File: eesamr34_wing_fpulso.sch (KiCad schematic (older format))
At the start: 19 parts, among them J3 Conn_01x02_Male, P1 SolderJumper_3_Bridged12, Q1 BS250, U2 4069

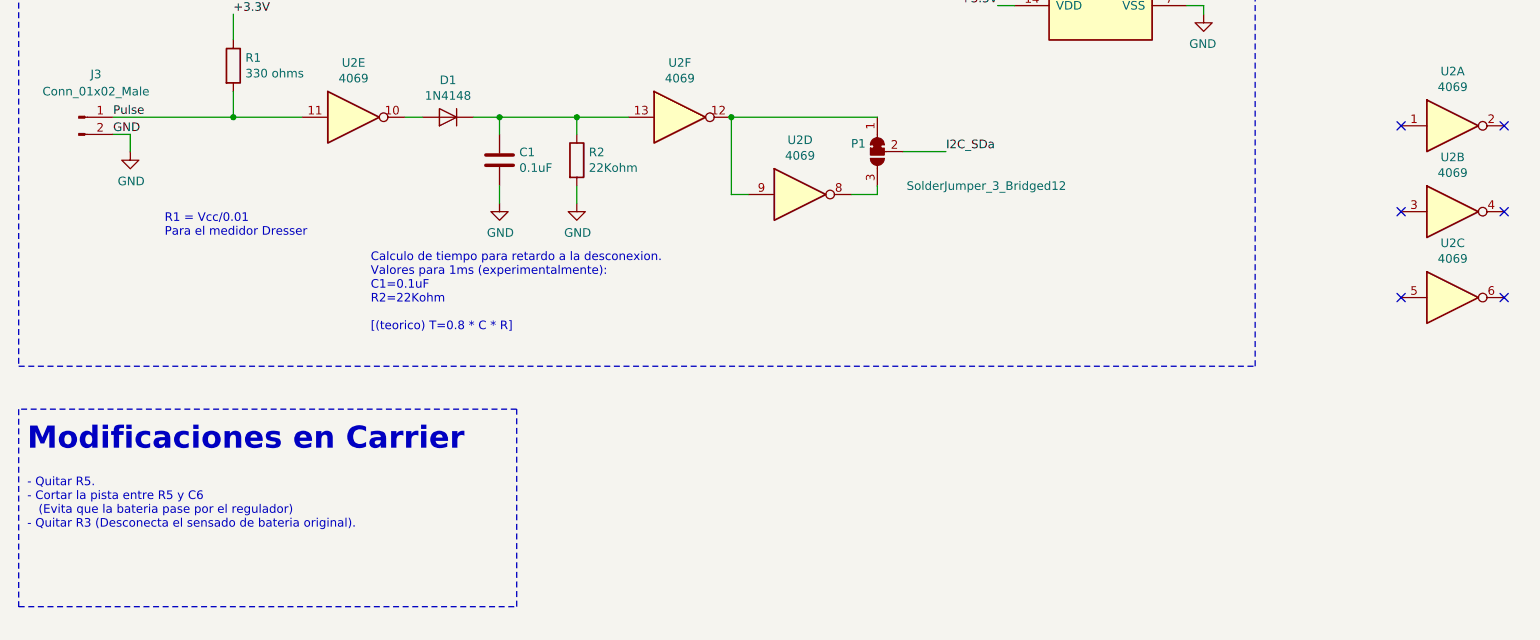
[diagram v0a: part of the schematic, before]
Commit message: entradas no usadas a 0
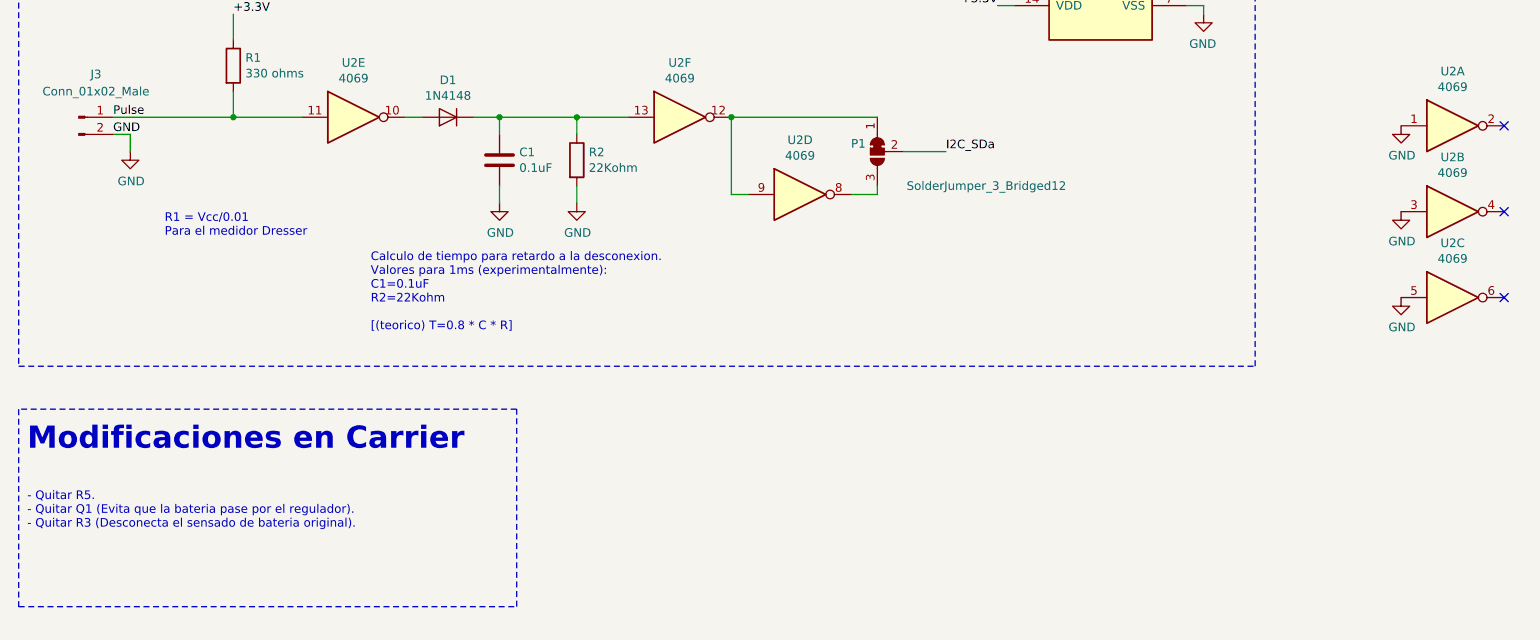
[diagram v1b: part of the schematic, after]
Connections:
- net GND: now also U2.1, U2.3, U2.5
- no-connect marks 26 -> 23
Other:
- note added: "- Quitar R5.\n- Quitar Q1 (Evita que la bateria pase por el regulador).\n- Quitar R3 (Desconecta el sensado de bateria original)."
- note removed: "- Quitar R5.\n- Cortar la pista entre R5 y C6 \n (Evita que la bateria pase por el regulador)\n- Quitar R3 (Desconecta el sensado de bateria original)."
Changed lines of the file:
@@
 ADC6
 Text Notes 600  9250 0    50   ~ 0
-- Quitar R5.\n- Cortar la pista entre R5 y C6 \n   (Evita que la bateria pase por el regulador)\n- Quitar R3 (Desconecta el sensado de bateria original).
+- Quitar R5.\n- Quitar Q1 (Evita que la bateria pase por el regulador).\n- Quitar R3 (Desconecta el sensado de bateria original).
 Text Notes 600  8800 0    129  ~ 26
 Modificaciones en Carrier\n
@@
 	1    0    0    -1
 $EndComp
-NoConn ~ 8600 6900
-NoConn ~ 8600 7400
-NoConn ~ 8600 7900
 NoConn ~ 9200 7900
 NoConn ~ 9200 7400
@@
 	1    0    0    -1
 $EndComp
+$Comp
+L power:GND #PWR?
+U 1 1 5F98C2FD
+P 8600 6900
+F 0 "#PWR?" H 8600 6650 50  0001 C CNN
+F 1 "GND" H 8605 6727 50  0000 C CNN
+F 2 "" H 8600 6900 50  0001 C CNN
+F 3 "" H 8600 6900 50  0001 C CNN
+	1    8600 6900
+	1    0    0    -1
+$EndComp
+$Comp
+L power:GND #PWR?
+U 1 1 5F98D849
+P 8600 7400
+F 0 "#PWR?" H 8600 7150 50  0001 C CNN
+F 1 "GND" H 8605 7227 50  0000 C CNN
+F 2 "" H 8600 7400 50  0001 C CNN
+F 3 "" H 8600 7400 50  0001 C CNN
+	1    8600 7400
+	1    0    0    -1
+$EndComp
+$Comp
+L power:GND #PWR?
+U 1 1 5F98E314
+P 8600 7900
+F 0 "#PWR?" H 8600 7650 50  0001 C CNN
+F 1 "GND" H 8605 7727 50  0000 C CNN
+F 2 "" H 8600 7900 50  0001 C CNN
+F 3 "" H 8600 7900 50  0001 C CNN
+	1    8600 7900
+	1    0    0    -1
+$EndComp

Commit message: cambios menores
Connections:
- net I2C_SDa: no longer P1.2 (C)
- net SPI_MOSI: now also P1.2 (C)
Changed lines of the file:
@@
 NoConn ~ 950  2550
 NoConn ~ 950  2350
-NoConn ~ 950  2250
+NoConn ~ 950  1950
 NoConn ~ 950  2150
 NoConn ~ 950  2050
 NoConn ~ 950  2450
-Text Label 5950 7050 0    50   ~ 0
-I2C_SDa
 Text Notes 600  950  0    129  ~ 26
 Shield Connection
@@
 	1    0    0    -1
 $EndComp
+Text Label 5950 7050 0    50   ~ 0
+SPI_MOSI
 $EndSCHEMATC
